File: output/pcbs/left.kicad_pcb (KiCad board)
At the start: 2 copper layers, 127.6 x 94 mm, 19 parts

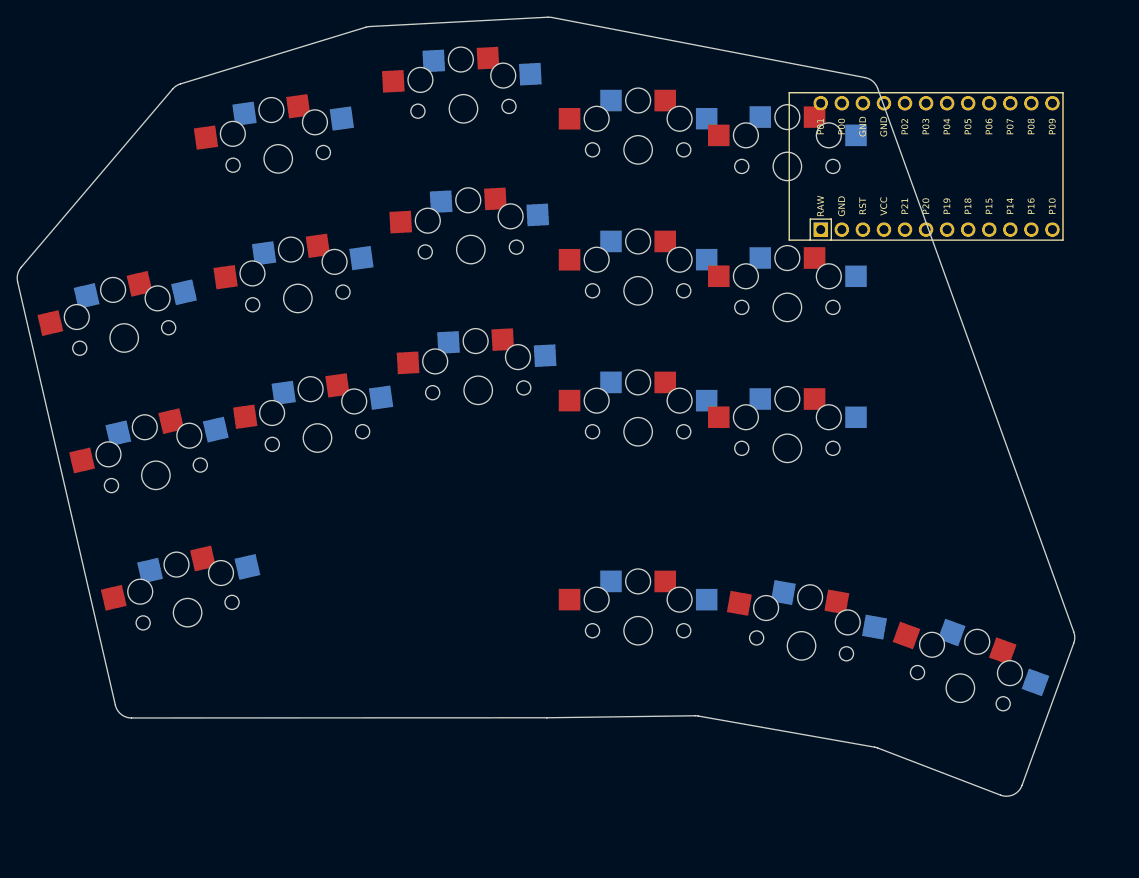
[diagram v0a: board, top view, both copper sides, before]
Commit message: Fix model names and generate
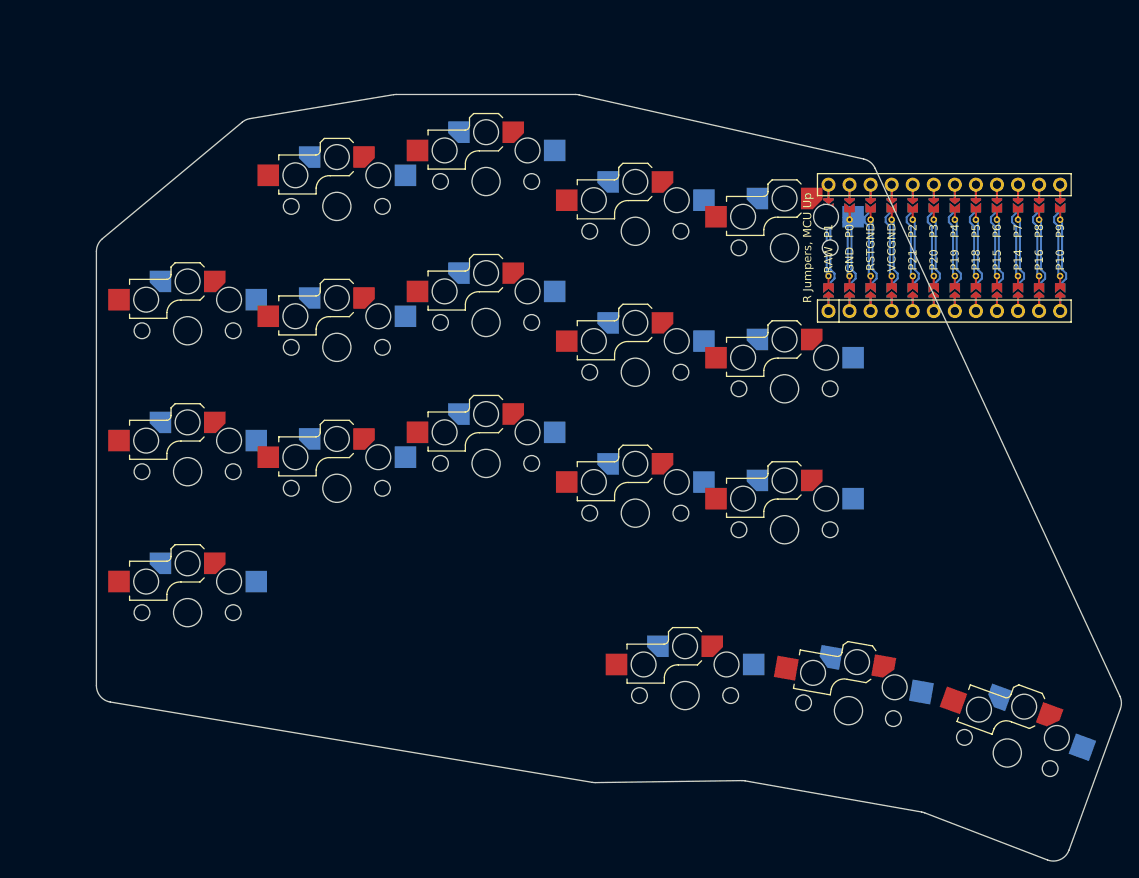
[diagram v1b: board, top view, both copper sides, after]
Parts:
- MCU1: footprint ProMicro -> ceoloide:mcu_nice_nano
- S1, S10, S11, S12, S13, S14, S15, S16, S17, S18, S2, S3, S4, S5, S6, S7, S8, S9: footprint PG1350 -> ceoloide:switch_choc_v1_v2; moved to B.Cu
- moved MCU1 9.83 mm to (90.0, -44.0), turned to 90 degrees
- moved S14 9.83 mm to (72.0, -27.0)
- moved S15 9.83 mm to (72.0, -44.0)
- moved S13 9.83 mm to (72.0, -10.0)
- moved S10 9.83 mm to (54.0, -12.0)
- moved S11 9.83 mm to (54.0, -29.0)
- moved S12 9.83 mm to (54.0, -46.0)
- moved S18 9.65 mm to (98.9, 16.9)
- moved S16 9.65 mm to (60.0, 10.0)
- moved S17 9.65 mm to (79.7, 11.8)
- moved S9 9.19 mm to (36.0, -52.0), turned to 0 degrees
- moved S6 9.10 mm to (18.0, -49.0), turned to 0 degrees
- moved S8 8.98 mm to (36.0, -35.0), turned to 0 degrees
- moved S7 8.87 mm to (36.0, -18.0), turned to 0 degrees
- moved S3 7.70 mm to (0.00, -34.0), turned to 0 degrees
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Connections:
- MCU1 pad 1: RAW -> MCU1_1
- MCU1 pad 10: P14 -> MCU1_10
- MCU1 pad 11: P16 -> MCU1_11
- MCU1 pad 12: P10 -> MCU1_12
- MCU1 pad 13: P1 -> MCU1_13
- MCU1 pad 14: P0 -> MCU1_14
- MCU1 pad 15: GND -> MCU1_15
- MCU1 pad 16: GND -> MCU1_16
- MCU1 pad 17: P2 -> MCU1_17
- MCU1 pad 18: P3 -> MCU1_18
- MCU1 pad 19: P4 -> MCU1_19
- MCU1 pad 2: GND -> MCU1_2
- MCU1 pad 20: P5 -> MCU1_20
- MCU1 pad 21: P6 -> MCU1_21
- MCU1 pad 22: P7 -> MCU1_22
- MCU1 pad 23: P8 -> MCU1_23
- MCU1 pad 24: P9 -> MCU1_24
- MCU1 pad 3: RST -> MCU1_3
- MCU1 pad 4: VCC -> MCU1_4
- MCU1 pad 5: P21 -> MCU1_5
- MCU1 pad 6: P20 -> MCU1_6
- MCU1 pad 7: P19 -> MCU1_7
- MCU1 pad 8: P18 -> MCU1_8
- MCU1 pad 9: P15 -> MCU1_9
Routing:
- net (no net): track 0.00 -> 337.7 mm
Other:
- board size 127.6 x 94 mm -> 123.6 x 92.5 mm
- net class Default removed

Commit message: Try to move MCU into place
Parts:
- moved MCU1 9.01 mm to (93.0, -52.5), turned to 0 degrees

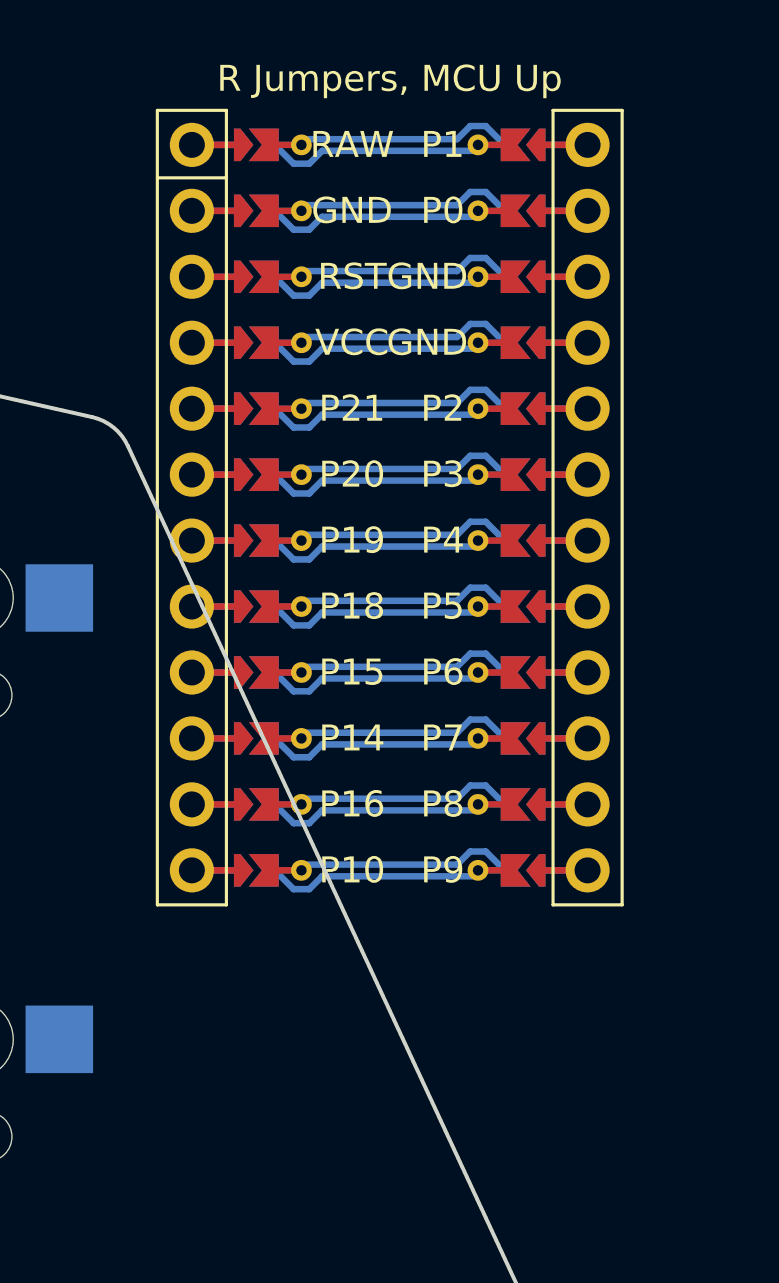
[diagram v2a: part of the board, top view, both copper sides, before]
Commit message: Reset MCU y placement just to see
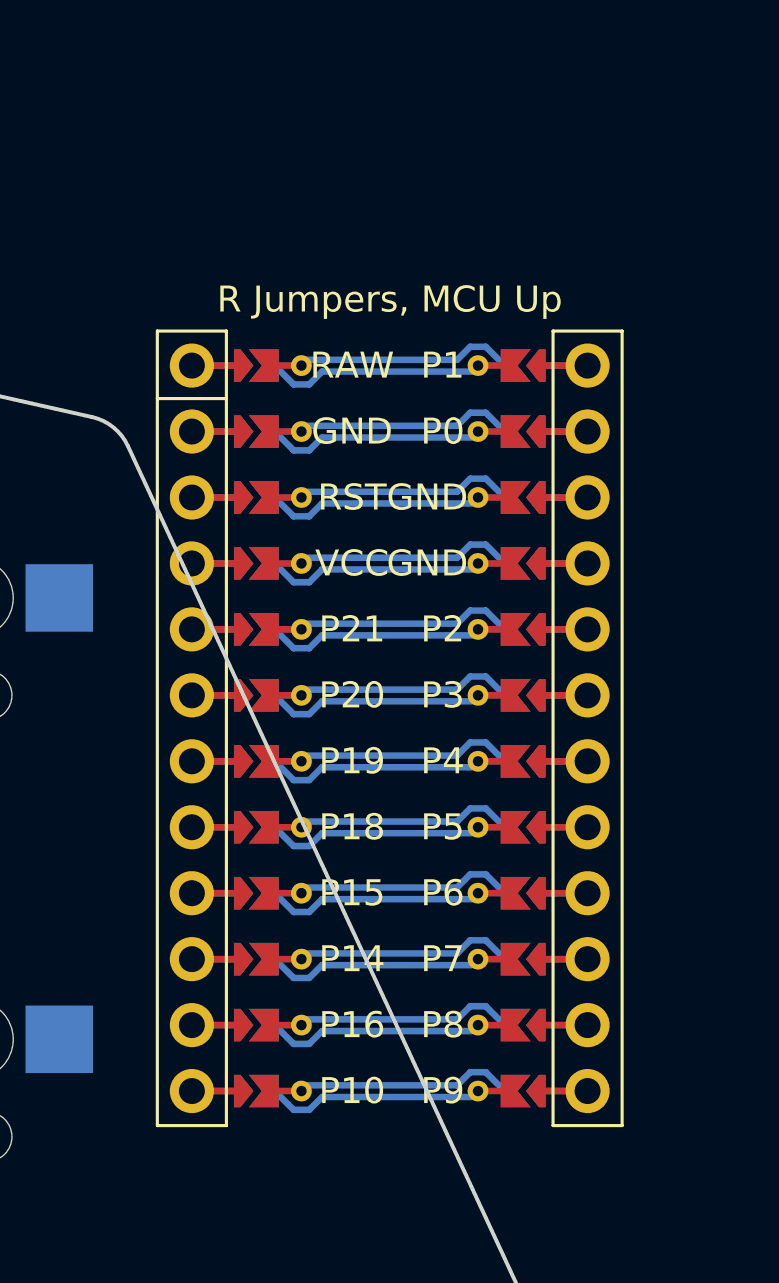
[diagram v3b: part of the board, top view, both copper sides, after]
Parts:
- moved MCU1 8.50 mm to (93.0, -44.0)

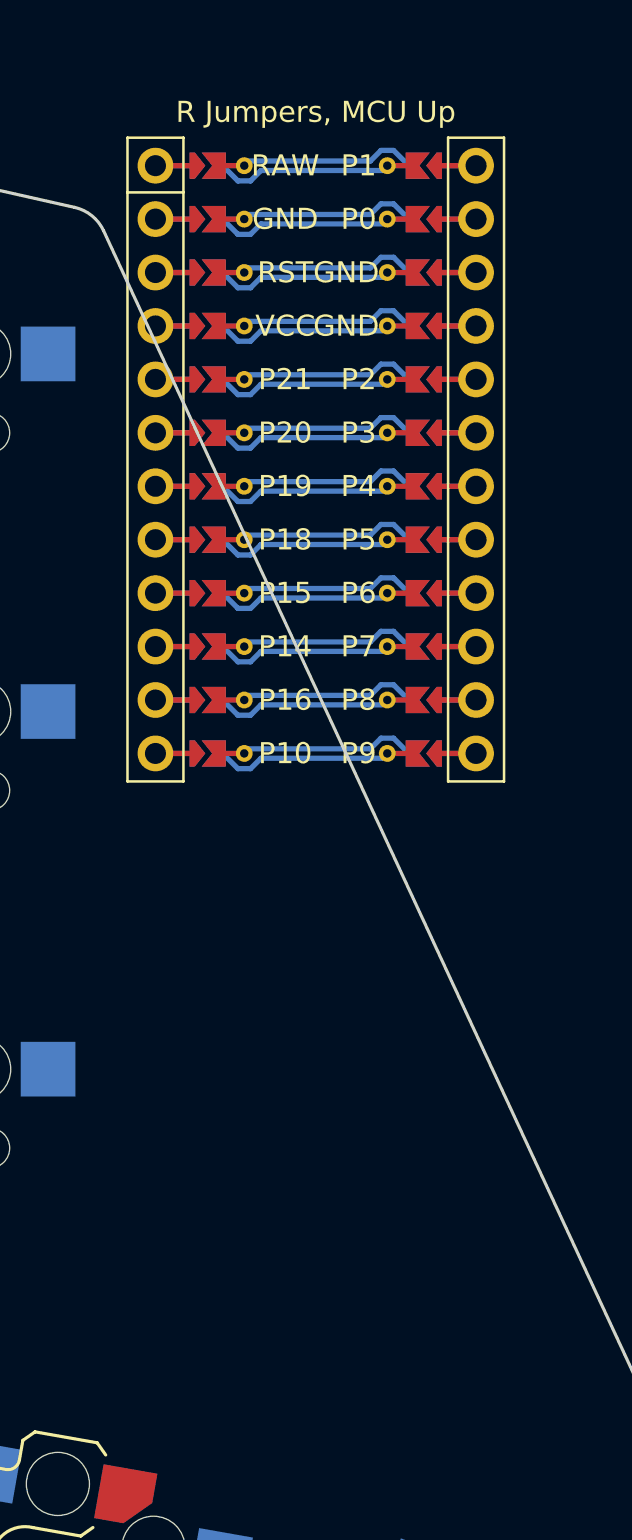
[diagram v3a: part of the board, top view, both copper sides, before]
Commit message: Shift MCU down 30mm
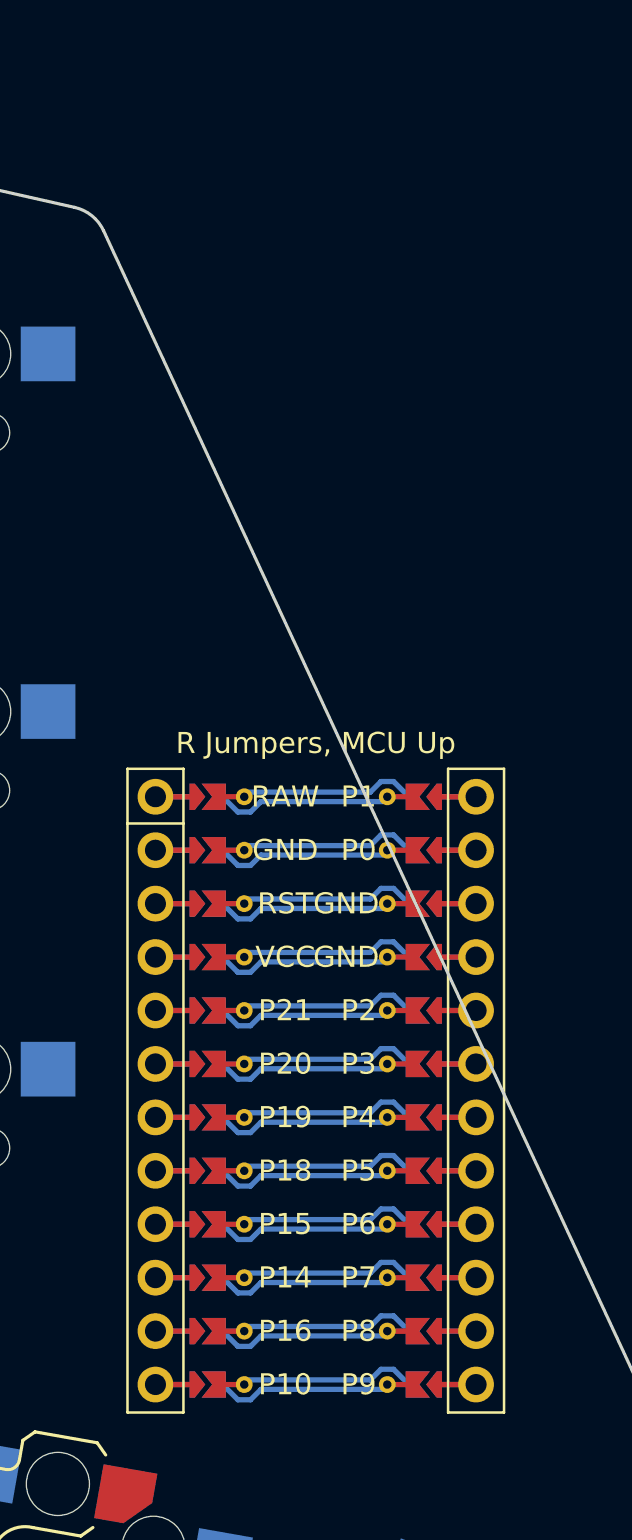
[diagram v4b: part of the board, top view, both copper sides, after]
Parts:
- moved MCU1 30.0 mm to (93.0, -14.0)

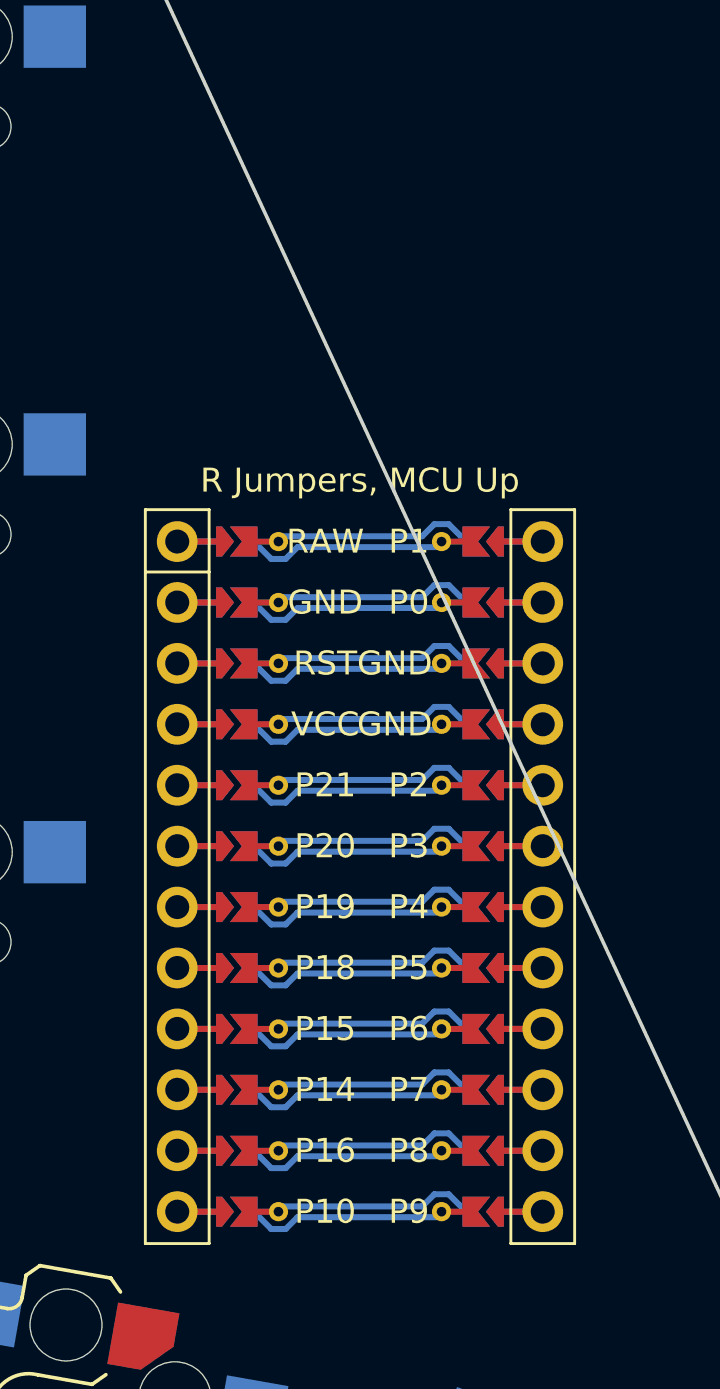
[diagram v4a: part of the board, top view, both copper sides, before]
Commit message: Shift MCU around a little more
-1 ky, and raise up the 3d model just for the preview
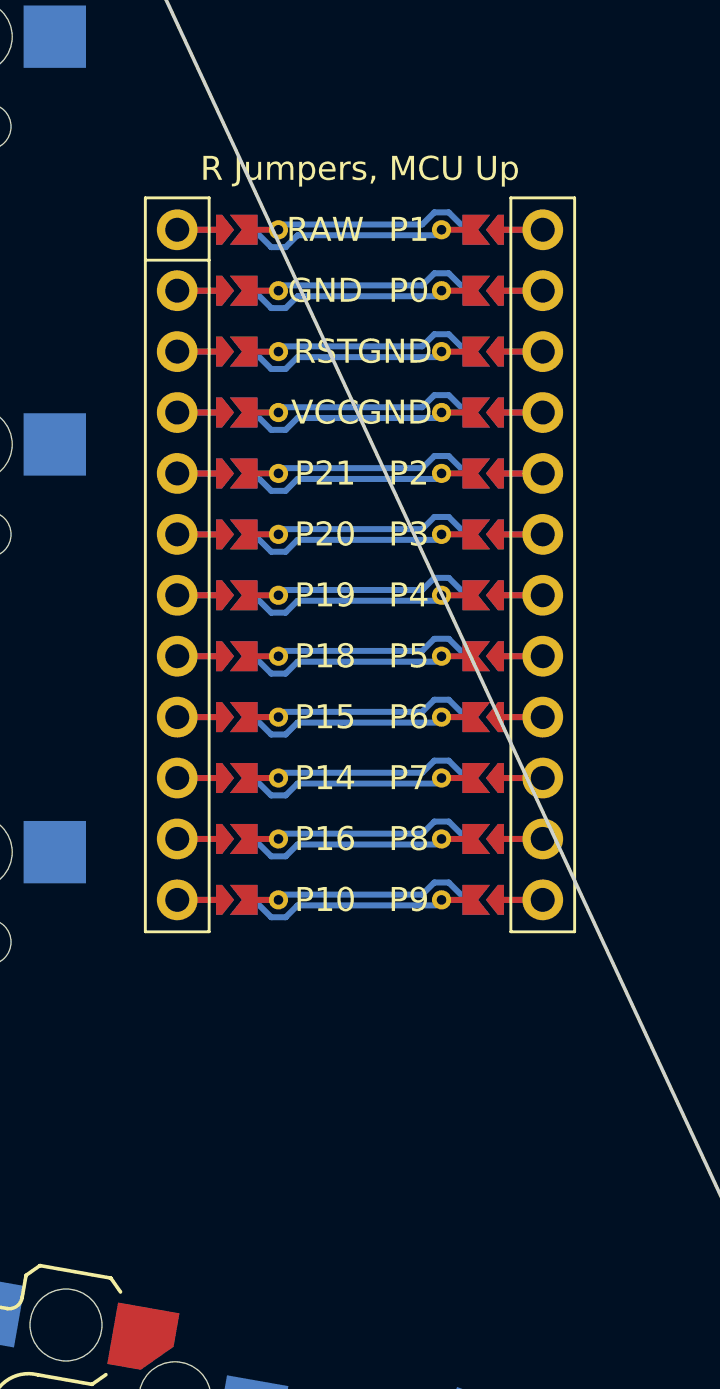
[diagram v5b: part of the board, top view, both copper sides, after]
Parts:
- moved MCU1 13.0 mm to (93.0, -27.0)

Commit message: More gentle tweaking
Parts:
- moved MCU1 18.0 mm to (93.0, -45.0)
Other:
- board size 123.6 x 92.5 mm -> 121.3 x 90.2 mm
